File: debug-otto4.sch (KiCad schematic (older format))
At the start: 1 part

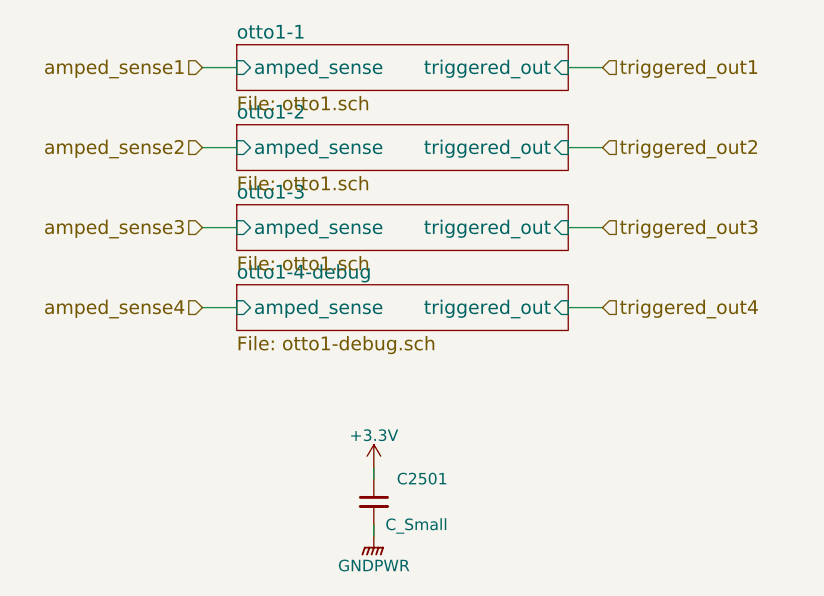
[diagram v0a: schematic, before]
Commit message: fixed debug pin going to multiple units
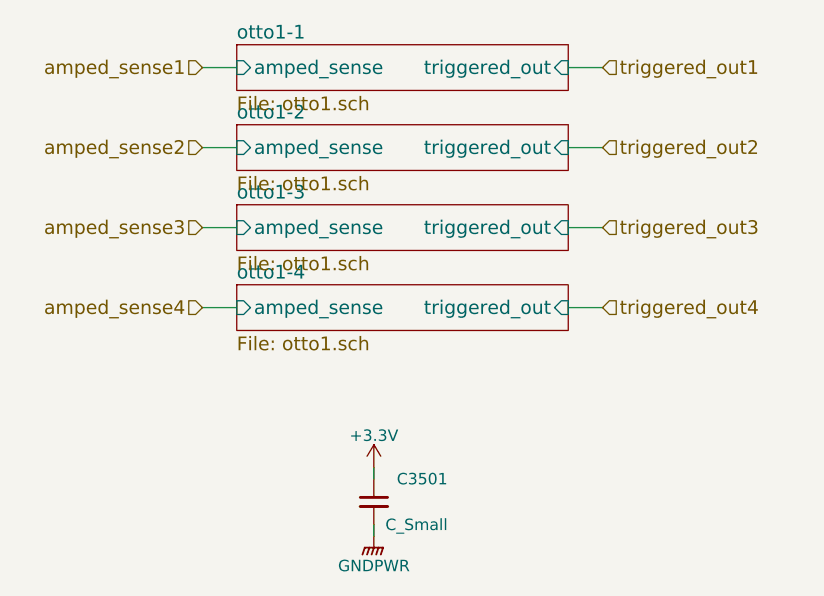
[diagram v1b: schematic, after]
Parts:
- renumbered C2501 to C3001
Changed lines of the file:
@@
 $Descr A4 11693 8268
 encoding utf-8
-Sheet 25 41
+Sheet 30 41
 Title ""
 Date ""
@@
 $Sheet
 S 1550 2100 1450 200
-U 5AFCD431
+U 5B023866
 F0 "otto1-2" 60
 F1 "otto1.sch" 60
@@
 $Sheet
 S 1550 2450 1450 200
-U 5AFCD50F
+U 5B023867
 F0 "otto1-3" 60
 F1 "otto1.sch" 60
@@
 $Sheet
 S 1550 2800 1450 200
-U 5AFCD579
-F0 "otto1-4-debug" 60
-F1 "otto1-debug.sch" 60
+U 5B023868
+F0 "otto1-4" 60
+F1 "otto1.sch" 60
 F2 "amped_sense" I L 1550 2900 60
 F3 "triggered_out" I R 3000 2900 60
@@
 	3000 2900 3150 2900
 $Comp
-L C_Small C2501
+L C_Small C3001
 U 1 1 5B007FCB
 P 2150 3750
-AR Path="/5AFCE970/5AFFB716/5AFCC2D5/5B007FCB" Ref="C2501"  Part="1"
 AR Path="/5AFCE970/5AFFB716/5AFCF0A3/5B007FCB" Ref="C3001"  Part="1"
 AR Path="/5AFCE970/5AFFB716/5AFD08C6/5B007FCB" Ref="C3501"  Part="1"
-F 0 "C2501" H 2250 3850 50  0000 L CNN
+F 0 "C3501" H 2250 3850 50  0000 L CNN
 F 1 "C_Small" H 2200 3650 50  0000 L CNN
 F 2 "Resistors_SMD:R_0805_HandSoldering" H 2150 3750 50  0001 C CNN
@@
 U 1 1 5B007FD7
 P 2150 3600
-AR Path="/5AFCE970/5AFFB716/5AFCC2D5/5B007FD7" Ref="#PWR?"  Part="1"
 AR Path="/5AFCE970/5AFFB716/5AFCF0A3/5B007FD7" Ref="#PWR?"  Part="1"
 AR Path="/5AFCE970/5AFFB716/5AFD08C6/5B007FD7" Ref="#PWR?"  Part="1"
@@
 U 1 1 5B0088D8
 P 2150 3900
-AR Path="/5AFCE970/5AFFB716/5AFCC2D5/5B0088D8" Ref="#PWR?"  Part="1"
 AR Path="/5AFCE970/5AFFB716/5AFCF0A3/5B0088D8" Ref="#PWR?"  Part="1"
 AR Path="/5AFCE970/5AFFB716/5AFD08C6/5B0088D8" Ref="#PWR?"  Part="1"
